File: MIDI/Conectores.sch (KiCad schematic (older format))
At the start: 4 parts, among them J4 CONN_01X06, J5 CONN_01X06

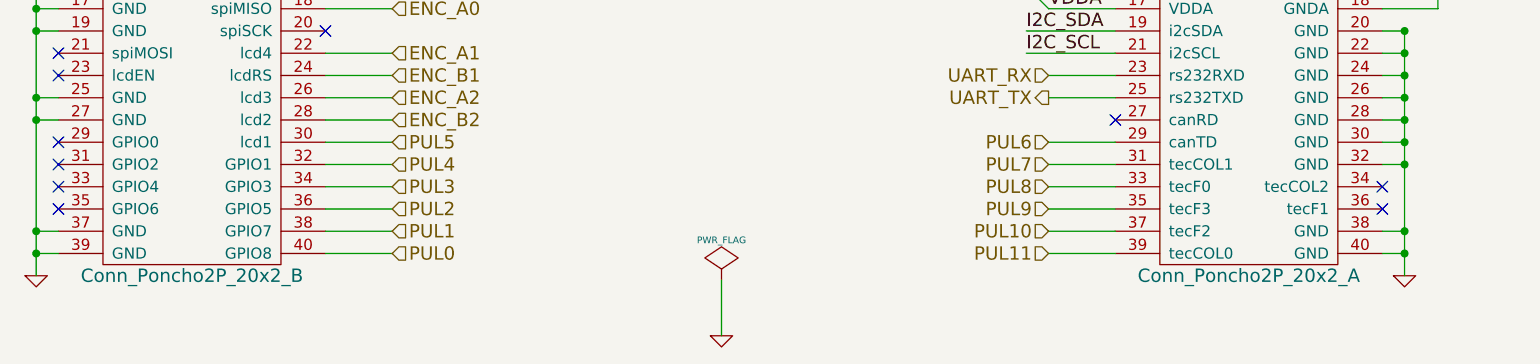
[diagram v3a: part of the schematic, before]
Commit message: Se modifican campos de componentes
> Se realizan los cambios en los campos de kiCost para reflejar los cambios de footprints (de 0603 a 0805).
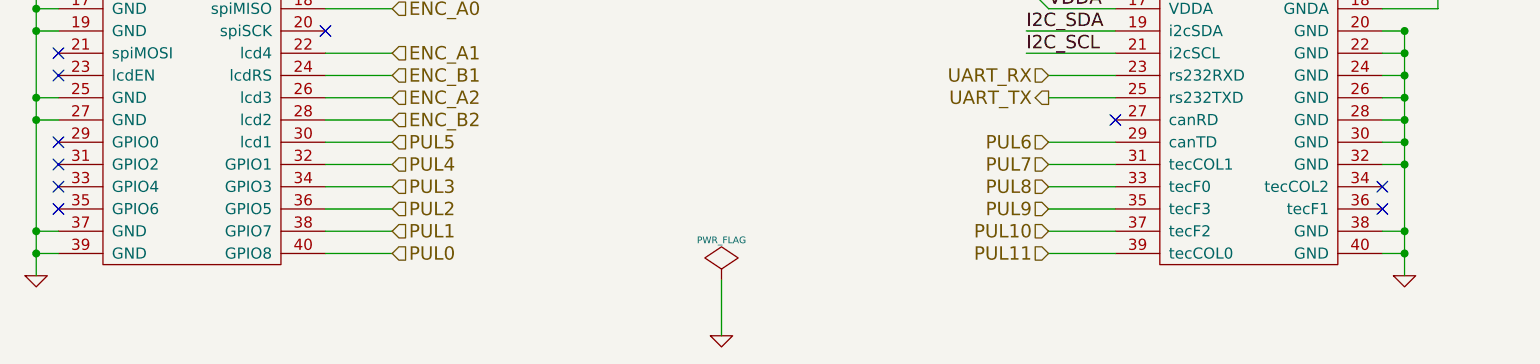
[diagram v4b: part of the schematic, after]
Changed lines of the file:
@@
 P 3095 3730
 F 0 "XB1" H 3395 4130 60  0000 C CNN
-F 1 "Conn_Poncho2P_20x2_B" H 3445 2030 60  0000 C CNN
+F 1 "Conn_Poncho2P_20x2_B" H 3445 2030 60  0001 C CNN
 F 2 "MIDI:PIN_ARRAY_20X2" H 3095 3730 60  0001 C CNN
 F 3 "http://portal.fciconnect.com/Comergent//fci/drawing/67996.pdf" H 3095 3730 60  0001 C CNN
@@
 P 7845 3730
 F 0 "XA1" H 8145 4130 60  0000 C CNN
-F 1 "Conn_Poncho2P_20x2_A" H 8195 2030 60  0000 C CNN
+F 1 "Conn_Poncho2P_20x2_A" H 8195 2030 60  0001 C CNN
 F 2 "MIDI:PIN_ARRAY_20X2" H 7845 3730 60  0001 C CNN
 F 3 "http://portal.fciconnect.com/Comergent//fci/drawing/67996.pdf" H 7845 3730 60  0001 C CNN

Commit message: Correcciones menores en campos para BOM
> Se corrigen error observados luego de la generación de la BOM.
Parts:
- J4: Description (none) -> CONN RCPT 6POS .100\" SGL PCB; Manf# 75915-306LF -> 75915-306LF
- J5: Description (none) -> CONN RCPT 6POS .100\" SGL PCB; Manf# 75916-306LF -> 75915-306LF
- XA1, XB1: Description (none) -> BERGSTIK II 0.100\" DUAL ST
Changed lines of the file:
@@
 F 2 "MIDI:Pin_Header_Straight_1x06_Pitch2.54mm" H 6595 2430 50  0001 C CNN
 F 3 "http://portal.fciconnect.com/Comergent//fci/drawing/75915.pdf" H 6595 2430 50  0001 C CNN
-F 4 "CONN RCPT 6POS .100\" SGL PCB" H 0   0   60  0001 C CNN "Desc"
+F 4 "CONN RCPT 6POS .100\" SGL PCB" H 0   0   60  0001 C CNN "Description"
 F 5 "609-3558-ND" H 0   0   50  0001 C CNN "Digikey#"
 F 6 "Amphenol FCI" H 0   0   50  0001 C CNN "Manf"
-F 7 "75916-306LF " H 0   0   50  0001 C CNN "Manf#"
+F 7 "75915-306LF" H 0   0   50  0001 C CNN "Manf#"
 F 8 "649-75915-306LF" H 0   0   50  0001 C CNN "Mouser#"
+F 9 "CONN RCPT 6POS .100\" SGL PCB" H 6595 2430 60  0001 C CNN "Desc"
 	1    6595 2430
 	-1   0    0    -1
@@
 F 2 "MIDI:Pin_Header_Straight_1x06_Pitch2.54mm" H 5045 2430 50  0001 C CNN
 F 3 "http://portal.fciconnect.com/Comergent//fci/drawing/75915.pdf" H 5045 2430 50  0001 C CNN
-F 4 "CONN RCPT 6POS .100\" SGL PCB" H 0   0   60  0001 C CNN "Desc"
+F 4 "CONN RCPT 6POS .100\" SGL PCB" H 0   0   60  0001 C CNN "Description"
 F 5 "609-3558-ND" H 0   0   50  0001 C CNN "Digikey#"
 F 6 "Amphenol FCI" H 0   0   50  0001 C CNN "Manf"
-F 7 "75915-306LF " H 0   0   50  0001 C CNN "Manf#"
+F 7 "75915-306LF" H 0   0   50  0001 C CNN "Manf#"
 F 8 "649-75915-306LF" H 0   0   50  0001 C CNN "Mouser#"
+F 9 "CONN RCPT 6POS .100\" SGL PCB" H 5045 2430 60  0001 C CNN "Desc"
 	1    5045 2430
 	1    0    0    -1
@@
 F 2 "MIDI:PIN_ARRAY_20X2" H 3095 3730 60  0001 C CNN
 F 3 "http://portal.fciconnect.com/Comergent//fci/drawing/67996.pdf" H 3095 3730 60  0001 C CNN
-F 4 "BERGSTIK II 0.100\" DUAL ST" H 0   0   60  0001 C CNN "Desc"
+F 4 "BERGSTIK II 0.100\" DUAL ST" H 0   0   60  0001 C CNN "Description"
 F 5 "609-4724-ND" H 0   0   50  0001 C CNN "Digikey#"
 F 6 "Amphenol FCI" H 0   0   50  0001 C CNN "Manf"
 F 7 "68602-140HLF" H 0   0   50  0001 C CNN "Manf#"
 F 8 "649-68602-140HLF" H 0   0   50  0001 C CNN "Mouser#"
+F 9 "BERGSTIK II 0.100\" DUAL ST" H 3095 3730 60  0001 C CNN "Desc"
 	1    3095 3730
 	1    0    0    -1
@@
 F 2 "MIDI:PIN_ARRAY_20X2" H 7845 3730 60  0001 C CNN
 F 3 "http://portal.fciconnect.com/Comergent//fci/drawing/67996.pdf" H 7845 3730 60  0001 C CNN
-F 4 "BERGSTIK II 0.100\" DUAL ST" H 0   0   60  0001 C CNN "Desc"
+F 4 "BERGSTIK II 0.100\" DUAL ST" H 0   0   60  0001 C CNN "Description"
 F 5 "609-4724-ND" H 0   0   50  0001 C CNN "Digikey#"
 F 6 "Amphenol FCI" H 0   0   50  0001 C CNN "Manf"
 F 7 "68602-140HLF" H 0   0   50  0001 C CNN "Manf#"
 F 8 "649-68602-140HLF" H 0   0   50  0001 C CNN "Mouser#"
+F 9 "BERGSTIK II 0.100\" DUAL ST" H 7845 3730 60  0001 C CNN "Desc"
 	1    7845 3730
 	1    0    0    -1

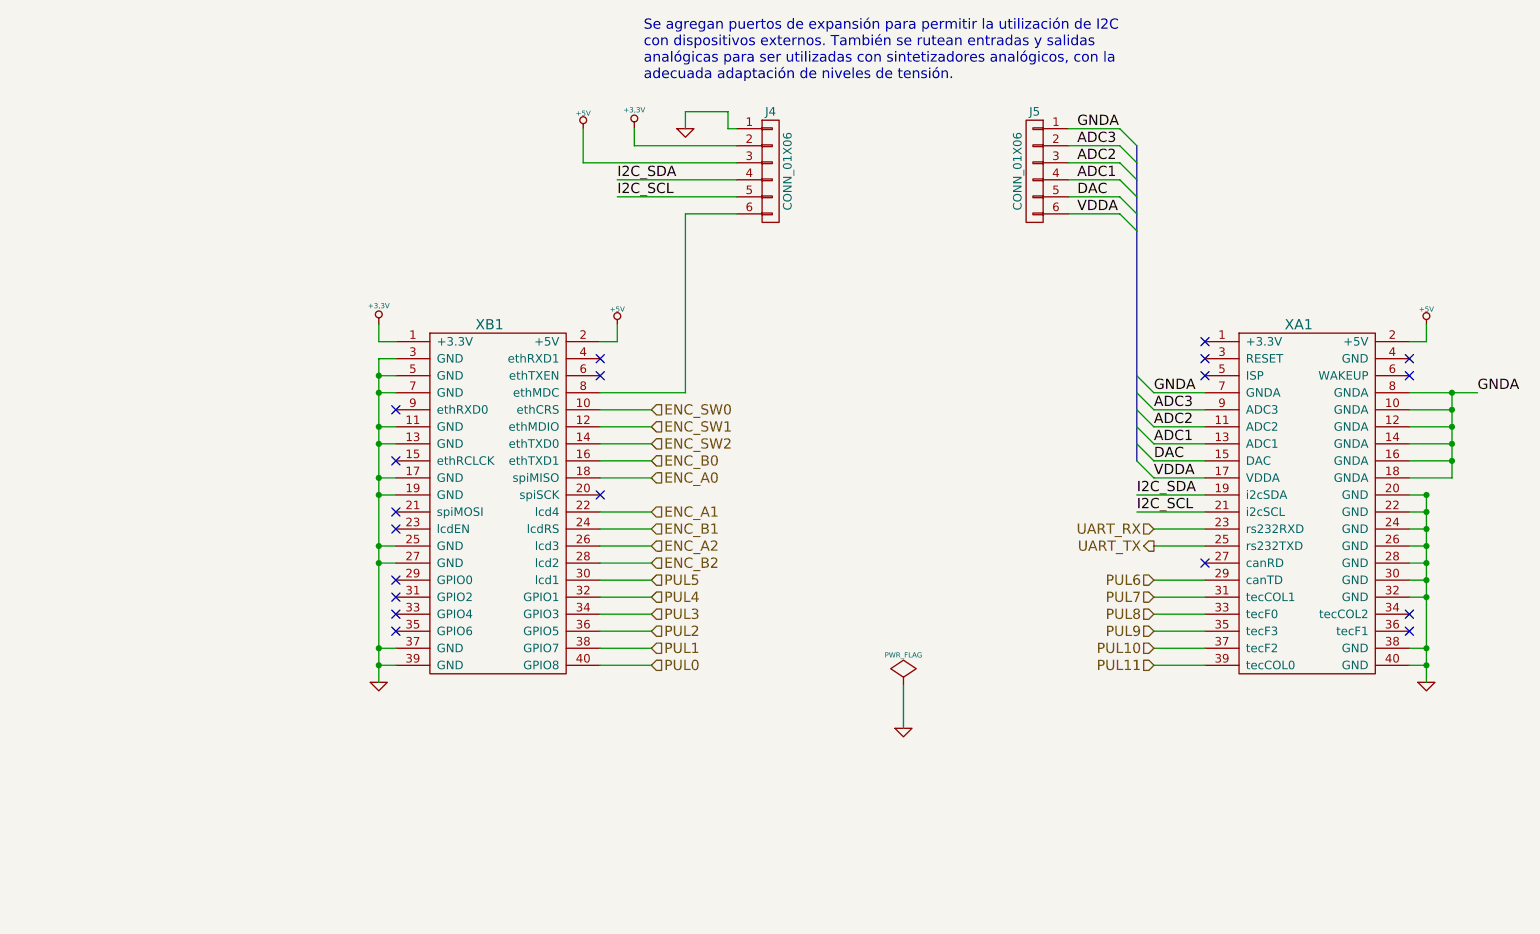
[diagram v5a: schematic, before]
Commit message: Se realizan cambios según revisiones
> Se realizan diversos cambios detallados en los respectivos archivos de revision (Moreno y Brengi 2da.) presentes en /Doc/Revisiones/.
> Se genera la versión 0.9 del circuito.
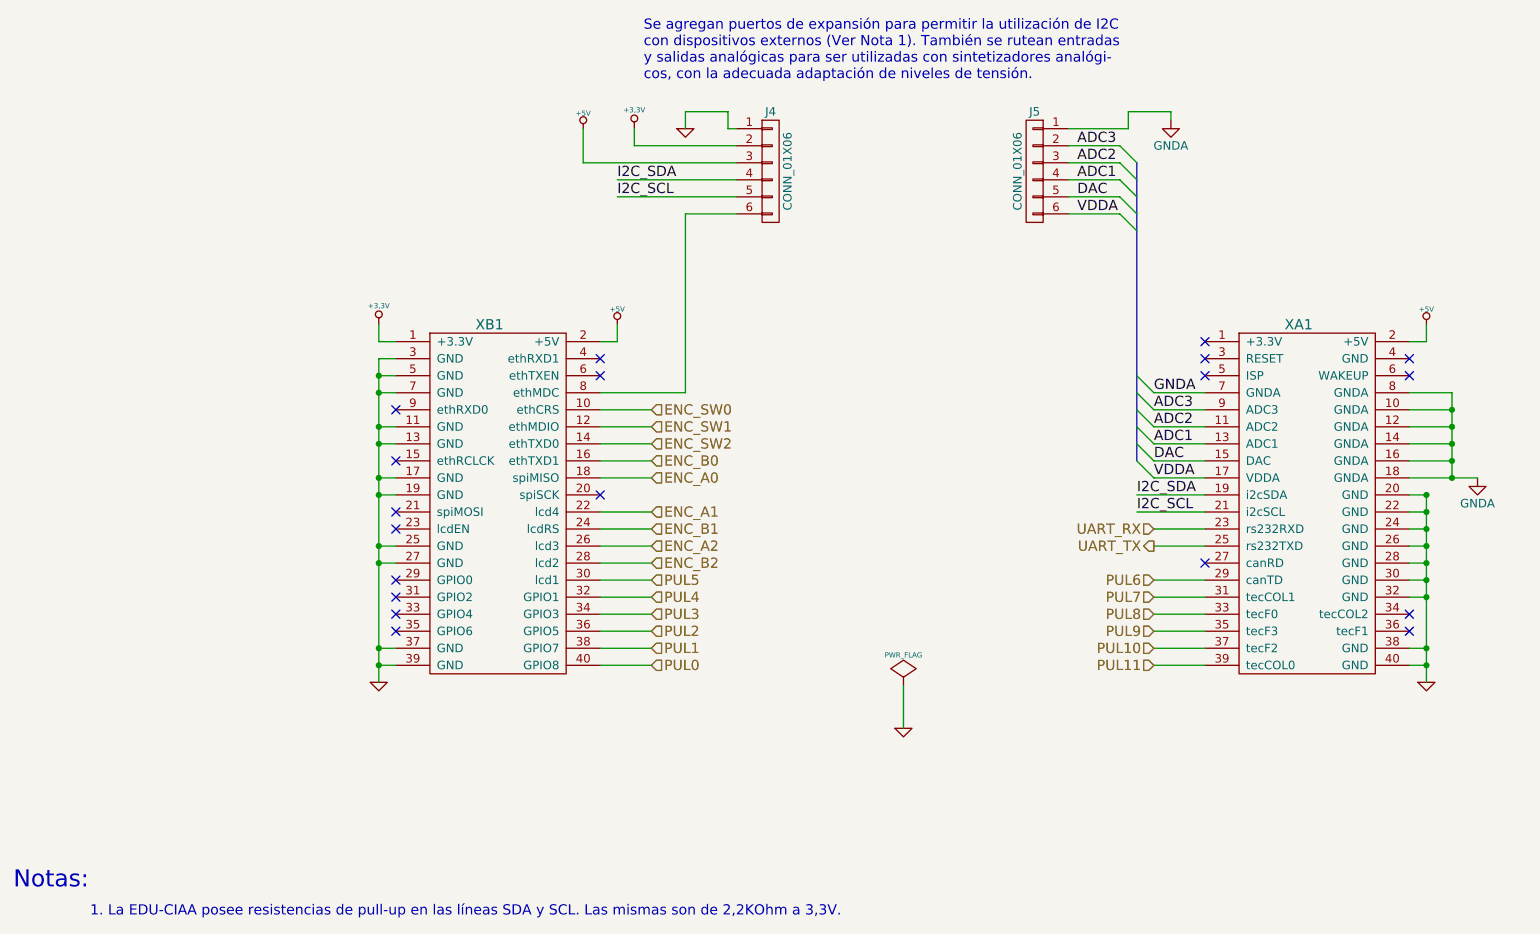
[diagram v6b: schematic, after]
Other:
- note added: "1. La EDU-CIAA posee resistencias de pull-up en las líneas SDA y SCL. Las mismas son de 2,2KOhm a 3,3V."
- note added: "Notas:"
- note added: "Se agregan puertos de expansión para permitir la utilización de I2C\ncon dispositivos externos (Ver Nota 1). También se rutean entradas\ny salidas analógicas para ser utilizadas con sintetizadores analógi-\ncos, con la adecuada adaptación de niveles de tensión."
- note removed: "Se agregan puertos de expansión para permitir la utilización de I2C\ncon dispositivos externos. También se rutean entradas y salidas\nanalógicas para ser utilizadas con sintetizadores analógicos, con la\nadecuada adaptación de niveles de tensión."
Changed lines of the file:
@@
 Sheet 3 5
 Title "Conectores"
-Date "2017-06-11"
-Rev "v0.2"
+Date "2017-08-13"
+Rev "v0.9"
 Comp "FIUBA - LSE - CESE  -  Diseño de Circuitos Impresos                       Licencia: BSD"
-Comment1 "Revisores: Marcelo Moreno  /  Diego Brengi"
+Comment1 "Revisor: Marcelo Moreno"
 Comment2 "Autor: Carlos I. Mancón"
 Comment3 ""
@@
 	1    0    0    -1
 $EndComp
-Text Label 6845 2180 0    60   ~ 0
-GNDA
 Text Label 6845 2280 0    60   ~ 0
 ADC3
@@
 Text Label 4145 2580 0    60   ~ 0
 I2C_SCL
-Text Label 9195 3730 0    60   ~ 0
-GNDA
 Text Notes 4300 1900 0    60   ~ 0
-Se agregan puertos de expansión para permitir la utilización de I2C\ncon dispositivos externos. También se rutean entradas y salidas\nanalógicas para ser utilizadas con sintetizadores analógicos, con la\nadecuada adaptación de niveles de tensión.
-Wire Bus Line
-	7195 2280 7195 4130
-Wire Wire Line
-	7295 3730 7595 3730
-Wire Wire Line
-	7295 3830 7595 3830
-Wire Wire Line
-	7295 3930 7595 3930
-Wire Wire Line
-	7295 4030 7595 4030
-Wire Wire Line
-	7295 4130 7595 4130
-Wire Wire Line
-	7295 4230 7595 4230
-Wire Wire Line
-	6795 2180 7095 2180
-Wire Wire Line
-	6795 2280 7095 2280
-Wire Wire Line
-	6795 2380 7095 2380
-Wire Wire Line
-	6795 2480 7095 2480
-Wire Wire Line
-	6795 2580 7095 2580
-Wire Wire Line
-	6795 2680 7095 2680
-Wire Wire Line
-	4045 4830 4345 4830
-Wire Wire Line
-	4045 4930 4345 4930
-Wire Wire Line
-	4045 5030 4345 5030
-Wire Wire Line
-	4045 5130 4345 5130
-Wire Wire Line
-	4045 5230 4345 5230
-Wire Wire Line
-	4045 5330 4345 5330
-Wire Wire Line
-	7295 4830 7595 4830
-Wire Wire Line
-	7295 4930 7595 4930
-Wire Wire Line
-	7295 5030 7595 5030
-Wire Wire Line
-	7295 5130 7595 5130
-Wire Wire Line
-	7295 5230 7595 5230
-Wire Wire Line
-	7295 5330 7595 5330
-Wire Wire Line
-	7595 4530 7295 4530
-Wire Wire Line
-	7295 4630 7595 4630
-Wire Wire Line
-	7595 4330 7195 4330
-Wire Wire Line
-	7595 4430 7195 4430
-Wire Wire Line
-	4345 3830 4045 3830
-Wire Wire Line
-	4045 3930 4345 3930
-Wire Wire Line
-	4345 4030 4045 4030
-Wire Wire Line
-	4045 4130 4345 4130
-Wire Wire Line
-	4345 4230 4045 4230
-Wire Wire Line
-	4045 4430 4345 4430
-Wire Wire Line
-	4345 4530 4045 4530
-Wire Wire Line
-	4045 4630 4345 4630
-Wire Wire Line
-	4345 4730 4045 4730
-Wire Wire Line
-	4245 2180 4245 2280
-Wire Wire Line
-	4245 2280 4845 2280
-Wire Wire Line
-	3945 2380 4845 2380
-Wire Wire Line
-	3945 2380 3945 2180
-Wire Wire Line
-	4845 2180 4795 2180
-Wire Wire Line
-	4795 2180 4795 2080
-Wire Wire Line
-	4795 2080 4545 2080
-Wire Wire Line
-	4545 2080 4545 2180
-Wire Wire Line
-	4145 2480 4845 2480
-Wire Wire Line
-	4145 2580 4845 2580
-Wire Wire Line
-	4045 3730 4545 3730
-Wire Wire Line
-	4545 3730 4545 2680
-Wire Wire Line
-	4545 2680 4845 2680
-Wire Wire Line
-	2745 3330 2745 3430
-Wire Wire Line
-	2745 3430 2845 3430
-Wire Wire Line
-	4045 3430 4145 3430
-Wire Wire Line
-	4145 3430 4145 3330
-Wire Wire Line
-	8795 3430 8895 3430
-Wire Wire Line
-	8795 5330 8895 5330
-Wire Wire Line
-	8795 5230 8895 5230
-Wire Wire Line
-	8795 4930 8895 4930
-Wire Wire Line
-	8795 4830 8895 4830
-Wire Wire Line
-	8795 4730 8895 4730
-Wire Wire Line
-	8795 4630 8895 4630
-Wire Wire Line
-	8795 4530 8895 4530
-Wire Wire Line
-	8795 4430 8895 4430
-Wire Wire Line
-	8795 4330 8895 4330
-Wire Wire Line
-	8795 3730 9195 3730
-Wire Wire Line
-	9045 4230 8795 4230
-Wire Wire Line
-	9045 3730 9045 4230
-Wire Wire Line
-	8795 4130 9045 4130
-Wire Wire Line
-	8795 4030 9045 4030
-Wire Wire Line
-	8795 3930 9045 3930
-Wire Wire Line
-	8795 3830 9045 3830
-Wire Wire Line
-	2845 3530 2745 3530
-Wire Wire Line
-	2745 3530 2745 5430
-Wire Wire Line
-	2845 5330 2745 5330
-Wire Wire Line
-	2845 5230 2745 5230
-Wire Wire Line
-	2845 4730 2745 4730
-Wire Wire Line
-	2845 4630 2745 4630
-Wire Wire Line
-	2845 4330 2745 4330
-Wire Wire Line
-	2845 4230 2745 4230
-Wire Wire Line
-	2845 4030 2745 4030
-Wire Wire Line
-	2845 3930 2745 3930
-Wire Wire Line
-	2845 3730 2745 3730
-Wire Wire Line
-	2845 3630 2745 3630
-Wire Wire Line
-	8895 3430 8895 3330
-Wire Wire Line
-	5825 5450 5825 5700
+Se agregan puertos de expansión para permitir la utilización de I2C\ncon dispositivos externos (Ver Nota 1). También se rutean entradas\ny salidas analógicas para ser utilizadas con sintetizadores analógi-\ncos, con la adecuada adaptación de niveles de tensión.
 Entry Wire Line
 	7195 3630 7295 3730
@@
 	7195 4130 7295 4230
 Entry Wire Line
-	7095 2180 7195 2280
-Entry Wire Line
 	7095 2280 7195 2380
 Entry Wire Line
@@
 Entry Wire Line
 	7095 2680 7195 2780
-Connection ~ 8895 5330
-Connection ~ 8895 5230
-Connection ~ 8895 4930
-Connection ~ 8895 4830
-Connection ~ 8895 4730
-Connection ~ 8895 4630
-Connection ~ 8895 4530
-Connection ~ 8895 4430
-Connection ~ 8895 4330
-Connection ~ 9045 3730
-Connection ~ 9045 4130
-Connection ~ 9045 4030
-Connection ~ 9045 3930
-Connection ~ 9045 3830
-Connection ~ 2745 5330
-Connection ~ 2745 5230
-Connection ~ 2745 4730
-Connection ~ 2745 4630
-Connection ~ 2745 4330
-Connection ~ 2745 4230
-Connection ~ 2745 4030
-Connection ~ 2745 3930
-Connection ~ 2745 3730
-Connection ~ 2745 3630
 NoConn ~ 8795 3630
 NoConn ~ 8795 5030
@@
 NoConn ~ 7595 3430
 NoConn ~ 8795 3530
+Text Notes 1050 6810 0    60   ~ 0
+1. La EDU-CIAA posee resistencias de pull-up en las líneas SDA y SCL. Las mismas son de 2,2KOhm a 3,3V.
+Text Notes 600  6650 0    100  ~ 0
+Notas:
+$Comp
+L GNDA #PWR?
+U 1 1 5990E91B
+P 9195 4230
+F 0 "#PWR?" H 9195 3980 50  0001 C CNN
+F 1 "GNDA" H 9195 4080 50  0000 C CNN
+F 2 "" H 9195 4230 50  0001 C CNN
+F 3 "" H 9195 4230 50  0001 C CNN
+	1    9195 4230
+	1    0    0    -1
+$EndComp
+Wire Wire Line
+	7295 3730 7595 3730
+Wire Wire Line
+	7295 3830 7595 3830
+Wire Wire Line
+	7295 3930 7595 3930
+Wire Wire Line
+	7295 4030 7595 4030
+Wire Wire Line
+	7295 4130 7595 4130
+Wire Wire Line
+	7295 4230 7595 4230
+Wire Wire Line
+	6795 2280 7095 2280
+Wire Wire Line
+	6795 2380 7095 2380
+Wire Wire Line
+	6795 2480 7095 2480
+Wire Wire Line
+	6795 2580 7095 2580
+Wire Wire Line
+	6795 2680 7095 2680
+Wire Wire Line
+	4045 4830 4345 4830
+Wire Wire Line
+	4045 4930 4345 4930
+Wire Wire Line
+	4045 5030 4345 5030
+Wire Wire Line
+	4045 5130 4345 5130
+Wire Wire Line
+	4045 5230 4345 5230
+Wire Wire Line
+	4045 5330 4345 5330
+Wire Wire Line
+	7295 4830 7595 4830
+Wire Wire Line
+	7295 4930 7595 4930
+Wire Wire Line
+	7295 5030 7595 5030
+Wire Wire Line
+	7295 5130 7595 5130
+Wire Wire Line
+	7295 5230 7595 5230
+Wire Wire Line
+	7295 5330 7595 5330
+Wire Wire Line
+	7595 4530 7295 4530
+Wire Wire Line
+	7295 4630 7595 4630
+Wire Wire Line
+	7595 4330 7195 4330
+Wire Wire Line
+	7595 4430 7195 4430
+Wire Wire Line
+	4345 3830 4045 3830
+Wire Wire Line
+	4045 3930 4345 3930
+Wire Wire Line
+	4345 4030 4045 4030
+Wire Wire Line
+	4045 4130 4345 4130
+Wire Wire Line
+	4345 4230 4045 4230
+Wire Wire Line
+	4045 4430 4345 4430
+Wire Wire Line
+	4345 4530 4045 4530
+Wire Wire Line
+	4045 4630 4345 4630
+Wire Wire Line
+	4345 4730 4045 4730
+Wire Wire Line
+	4245 2180 4245 2280
+Wire Wire Line
+	4245 2280 4845 2280
+Wire Wire Line
+	3945 2380 4845 2380
+Wire Wire Line
+	3945 2380 3945 2180
+Wire Wire Line
+	4845 2180 4795 2180
+Wire Wire Line
+	4795 2180 4795 2080
+Wire Wire Line
+	4795 2080 4545 2080
+Wire Wire Line
+	4545 2080 4545 2180
+Wire Wire Line
+	4145 2480 4845 2480
+Wire Wire Line
+	4145 2580 4845 2580
+Wire Wire Line
+	4045 3730 4545 3730
+Wire Wire Line
+	4545 3730 4545 2680
+Wire Wire Line
+	4545 2680 4845 2680
+Wire Wire Line
+	2745 3330 2745 3430
+Wire Wire Line
+	2745 3430 2845 3430
+Wire Wire Line
+	4045 3430 4145 3430
+Wire Wire Line
+	4145 3430 4145 3330
+Wire Wire Line
+	8795 3430 8895 3430
+Wire Wire Line
+	8795 5330 8895 5330
+Wire Wire Line
+	8795 5230 8895 5230
+Wire Wire Line
+	8795 4930 8895 4930
+Wire Wire Line
+	8795 4830 8895 4830
+Wire Wire Line
+	8795 4730 8895 4730
+Wire Wire Line
+	8795 4630 8895 4630
+Wire Wire Line
+	8795 4530 8895 4530
+Wire Wire Line
+	8795 4430 8895 4430
+Wire Wire Line
+	8795 4330 8895 4330
+Wire Wire Line
+	8795 4230 9195 4230
+Wire Wire Line
+	9045 3730 9045 4230
+Wire Wire Line
+	8795 4130 9045 4130
+Wire Wire Line
+	8795 4030 9045 4030
+Wire Wire Line
+	8795 3930 9045 3930
+Wire Wire Line
+	8795 3830 9045 3830
+Wire Wire Line
+	2845 3530 2745 3530
+Wire Wire Line
+	2745 3530 2745 5430
+Wire Wire Line
+	2845 5330 2745 5330
+Wire Wire Line
+	2845 5230 2745 5230
+Wire Wire Line
+	2845 4730 2745 4730
+Wire Wire Line
+	2845 4630 2745 4630
+Wire Wire Line
+	2845 4330 2745 4330
+Wire Wire Line
+	2845 4230 2745 4230
+Wire Wire Line
+	2845 4030 2745 4030
+Wire Wire Line
+	2845 3930 2745 3930
+Wire Wire Line
+	2845 3730 2745 3730
+Wire Wire Line
+	2845 3630 2745 3630
+Wire Wire Line
+	8895 3430 8895 3330
+Wire Wire Line
+	5825 5450 5825 5700
+Connection ~ 8895 5330
+Connection ~ 8895 5230
+Connection ~ 8895 4930
+Connection ~ 8895 4830
+Connection ~ 8895 4730
+Connection ~ 8895 4630
+Connection ~ 8895 4530
+Connection ~ 8895 4430
+Connection ~ 8895 4330
+Connection ~ 9045 4130
+Connection ~ 9045 4030
+Connection ~ 9045 3930
+Connection ~ 9045 3830
+Connection ~ 2745 5330
+Connection ~ 2745 5230
+Connection ~ 2745 4730
+Connection ~ 2745 4630
+Connection ~ 2745 4330
+Connection ~ 2745 4230
+Connection ~ 2745 4030
+Connection ~ 2745 3930
+Connection ~ 2745 3730
+Connection ~ 2745 3630
 Wire Wire Line
 	8895 4330 8895 5430
+Connection ~ 9045 4230
+Wire Wire Line
+	8795 3730 9045 3730
+Wire Bus Line
+	7195 2380 7195 4130
+$Comp
+L GNDA #PWR?
+U 1 1 5990EC64
+P 7395 2130
+F 0 "#PWR?" H 7395 1880 50  0001 C CNN
+F 1 "GNDA" H 7395 1980 50  0000 C CNN
+F 2 "" H 7395 2130 50  0001 C CNN
+F 3 "" H 7395 2130 50  0001 C CNN
+	1    7395 2130
+	1    0    0    -1
+$EndComp
+Wire Wire Line
+	7395 2130 7395 2080
+Wire Wire Line
+	7395 2080 7145 2080
+Wire Wire Line
+	7145 2080 7145 2180
+Wire Wire Line
+	7145 2180 6795 2180
 $EndSCHEMATC
